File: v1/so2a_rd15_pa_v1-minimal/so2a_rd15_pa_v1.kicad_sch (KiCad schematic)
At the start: 56 parts, among them J1 RF_in, J2 RF_out, Q1 RD15HVF1, Q2 MMBT3904, U1 L78L05_SOT89

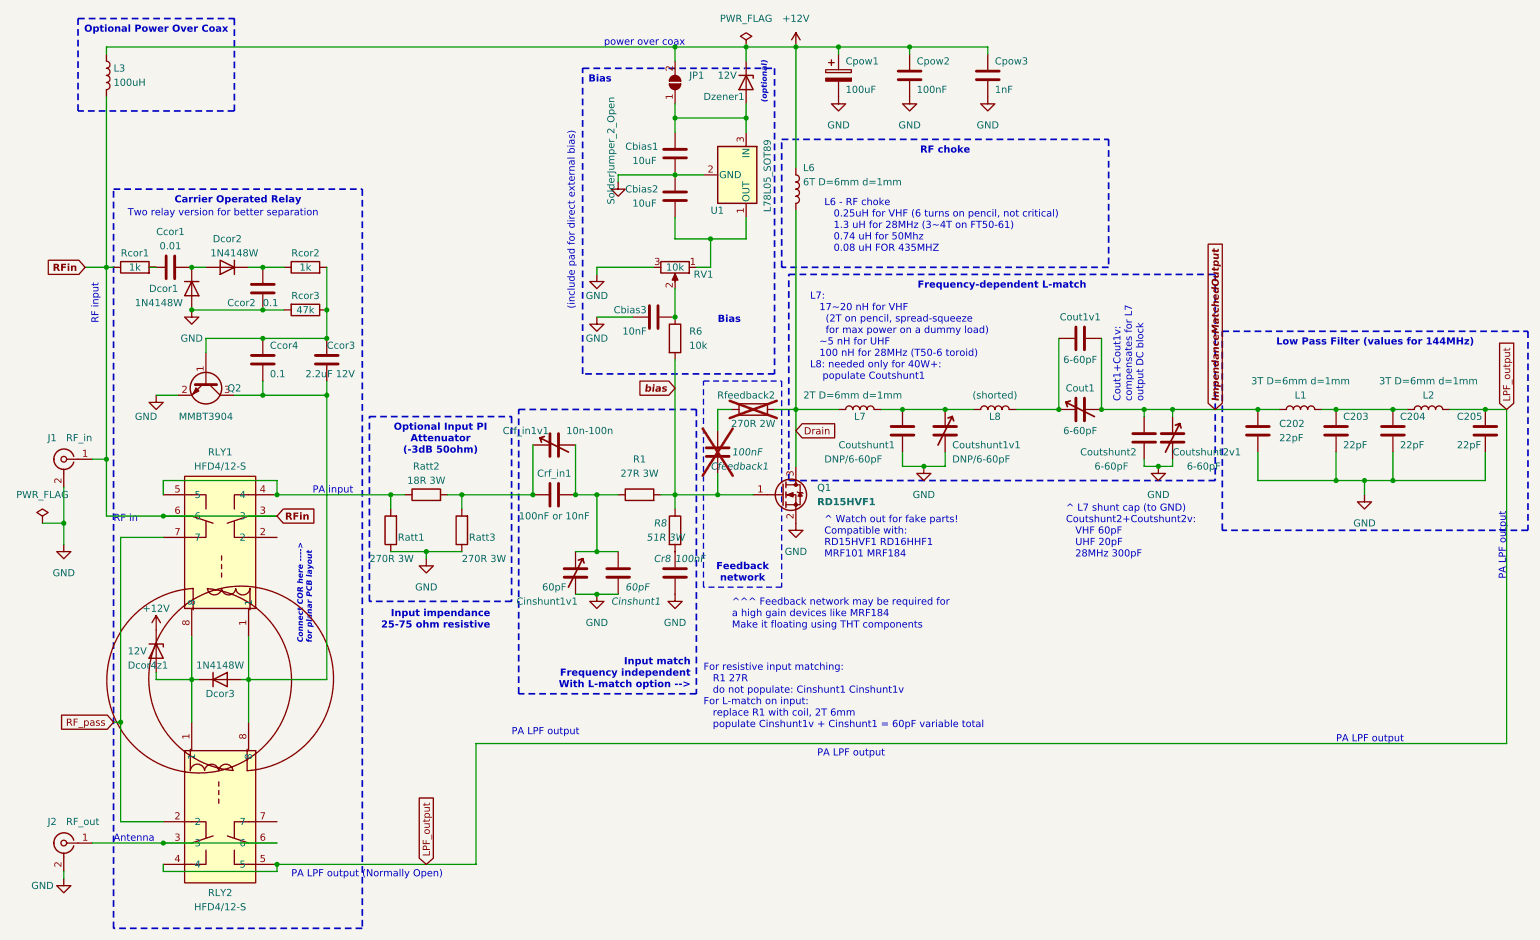
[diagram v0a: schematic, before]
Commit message: v0.3.1: Adding minimal board; changes for the drain trace width
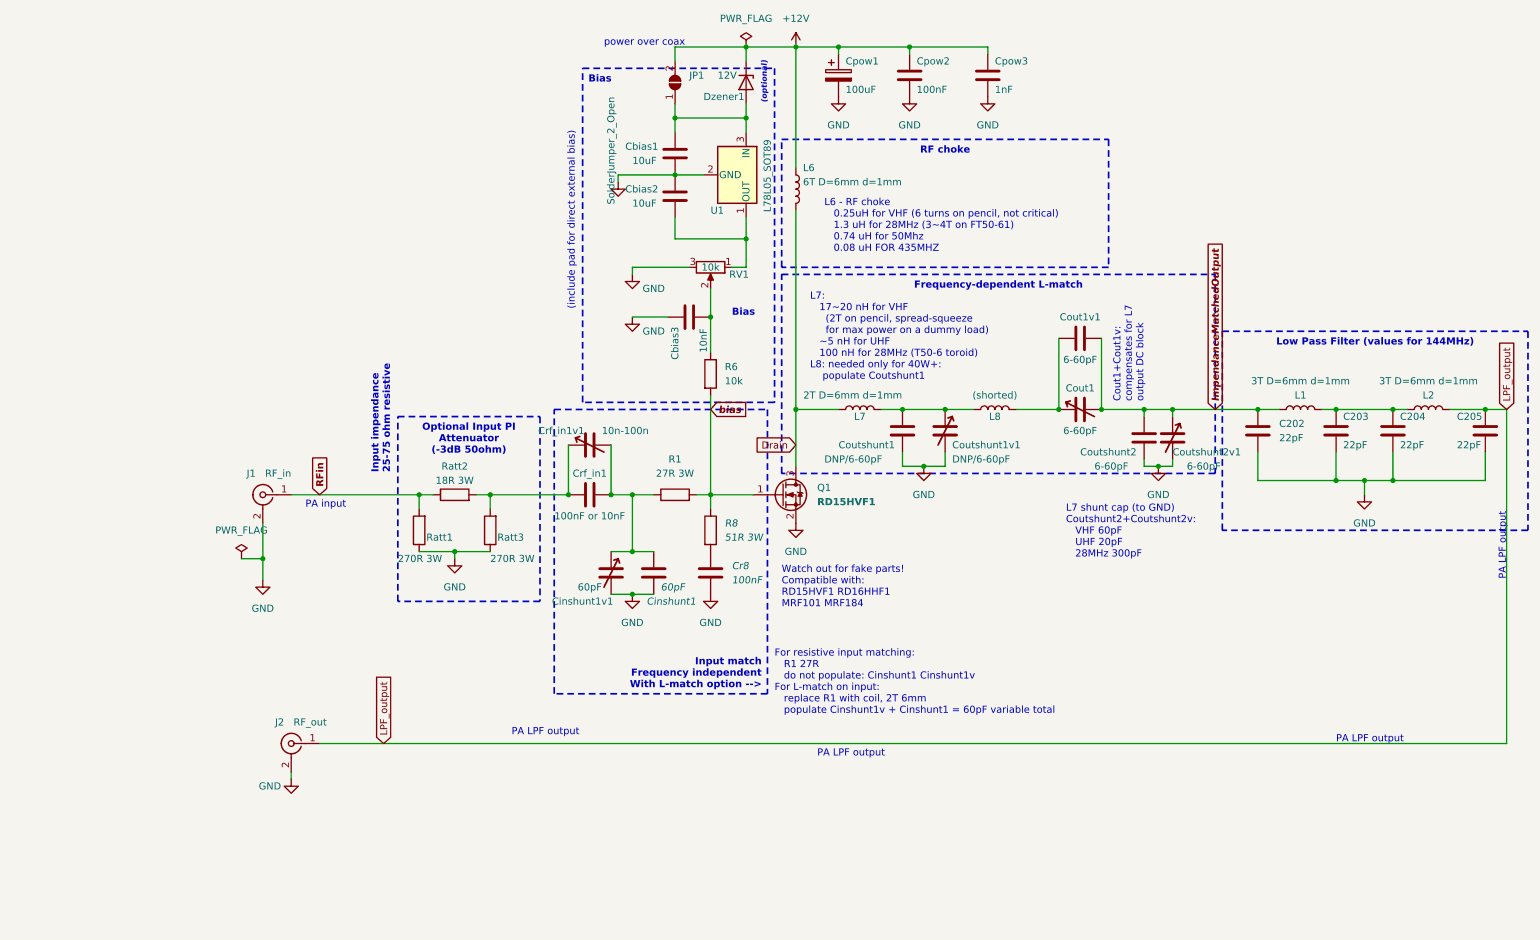
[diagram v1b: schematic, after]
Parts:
- removed Ccor1: 0.01, Capacitor_SMD:C_1206_3216Metric, symbol Device:C
- removed Ccor2, Ccor4: 0.1, Capacitor_SMD:C_1206_3216Metric, symbol Device:C
- removed Ccor3: 2.2uF 12V, Capacitor_SMD:C_1206_3216Metric, symbol Device:C
- removed Cfeedback1: 100nF, Capacitor_SMD:C_1206_3216Metric, symbol Device:C
- removed Dcor1, Dcor2, Dcor3: 1N4148W, Diode_SMD:D_SOD-123, symbol Diode:1N4148W
- removed Dcor4z1: 12V, Diode_SMD:D_SOD-123, symbol Device:D_Zener
- removed L3: 100uH, Inductor_SMD:L_Wuerth_HCM-1050, symbol Device:L
- removed Q2: MMBT3904, Package_TO_SOT_SMD:SOT-23, symbol Transistor_BJT:MMBT3904
- removed RLY1, RLY2: HFD4/12-S, custom2:RELAY-SMD_HFD4-XX-SR, symbol custom:HFD4_12-S
- removed Rcor1, Rcor2: 1k, Resistor_SMD:R_0805_2012Metric, symbol Device:R
- removed Rcor3: 47k, Resistor_SMD:R_0805_2012Metric, symbol Device:R
- removed Rfeedback2: 270R 2W, Resistor_SMD:R_2010_5025Metric, symbol Device:R
- R8: value 51R 3W -> 51R 3W
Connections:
- net LPF_output: now also J2.1 (In)
- net RFin: now also Ratt1.2, Ratt2.1
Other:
- note added: "L7 shunt cap (to GND) Coutshunt2+Coutshunt2v: VHF 60pF UHF 20pF 28MHz 300pF"
- note added: "Watch out for fake parts! Compatible with: RD15HVF1 RD16HHF1 MRF101 MRF184"
- note removed: "Antenna"
- note removed: "Connect COR here ----> for planar PCB layout"
- note removed: "PA LPF output (Normally Open)"
- note removed: "RF in"
- note removed: "RF input"
- note removed: "Two relay version for better separation"
- note removed: "^ L7 shunt cap (to GND) Coutshunt2+Coutshunt2v: VHF 60pF UHF 20pF 28MHz 300pF"
- note removed: "^ Watch out for fake parts! Compatible with: RD15HVF1 RD16HHF1 MRF101 MRF184"
- note removed: "^^^ Feedback network may be required for a high gain devices like MRF184 Make it floating using THT components"
- title: Universal HamBrewers amplifier PCB -> MINIMAL Universal HamBrewers amplifier PCB
- moved on the sheet: Cbias3, Cinshunt1, Cinshunt1v1, Cr8, Crf_in1, Crf_in1v1, J1, J2, R1, R6, R8, RV1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
